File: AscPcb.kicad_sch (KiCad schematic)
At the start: 30 parts, among them J1 USB_C_Receptacle_USB2.0_16P, J2 B2B-PH-K-S, SW1 SW_MEC_5E, SW2 SW_MEC_5E, U1 TLV75801PDRV, U2 BQ24040DSQR, U3 ESP32-C3-WROOM-02

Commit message: schematic first attempt
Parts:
- removed C10, C11: 100nF, Capacitor_SMD:C_0603_1608Metric, symbol Device:C
- removed C12, C5: 20uF, Capacitor_SMD:C_0603_1608Metric, symbol Device:C
- added R10, R11, R12, R9: 10k, Resistor_SMD:R_0603_1608Metric, symbol Device:R
- C8, C9: value C -> 1uF
- SW1: value SW_MEC_5E -> RESET
- SW2: value SW_MEC_5E -> BOOT
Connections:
- net 3V3: now also R10.1, R11.1, R12.2, R9.1
- net GND: now also C8.2, C9.2, SW1.1, SW1.2, SW2.1, SW2.2
- net at C9.1: now also SW2.3 (K), SW2.4 (A), U3.8 (IO9), R10.2
- net at U3.16 (IO2): now also R12.1
- net at U3.2 (EN): now also C8.1, SW1.3 (K), SW1.4 (A), R9.2
- net at U3.7 (IO8): now also R11.2
- net USB_N renamed D-
- net USB_P renamed D+
- no-connect marks 0 -> 15
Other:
- moved on the sheet: C8, C9, SW1, SW2, U3

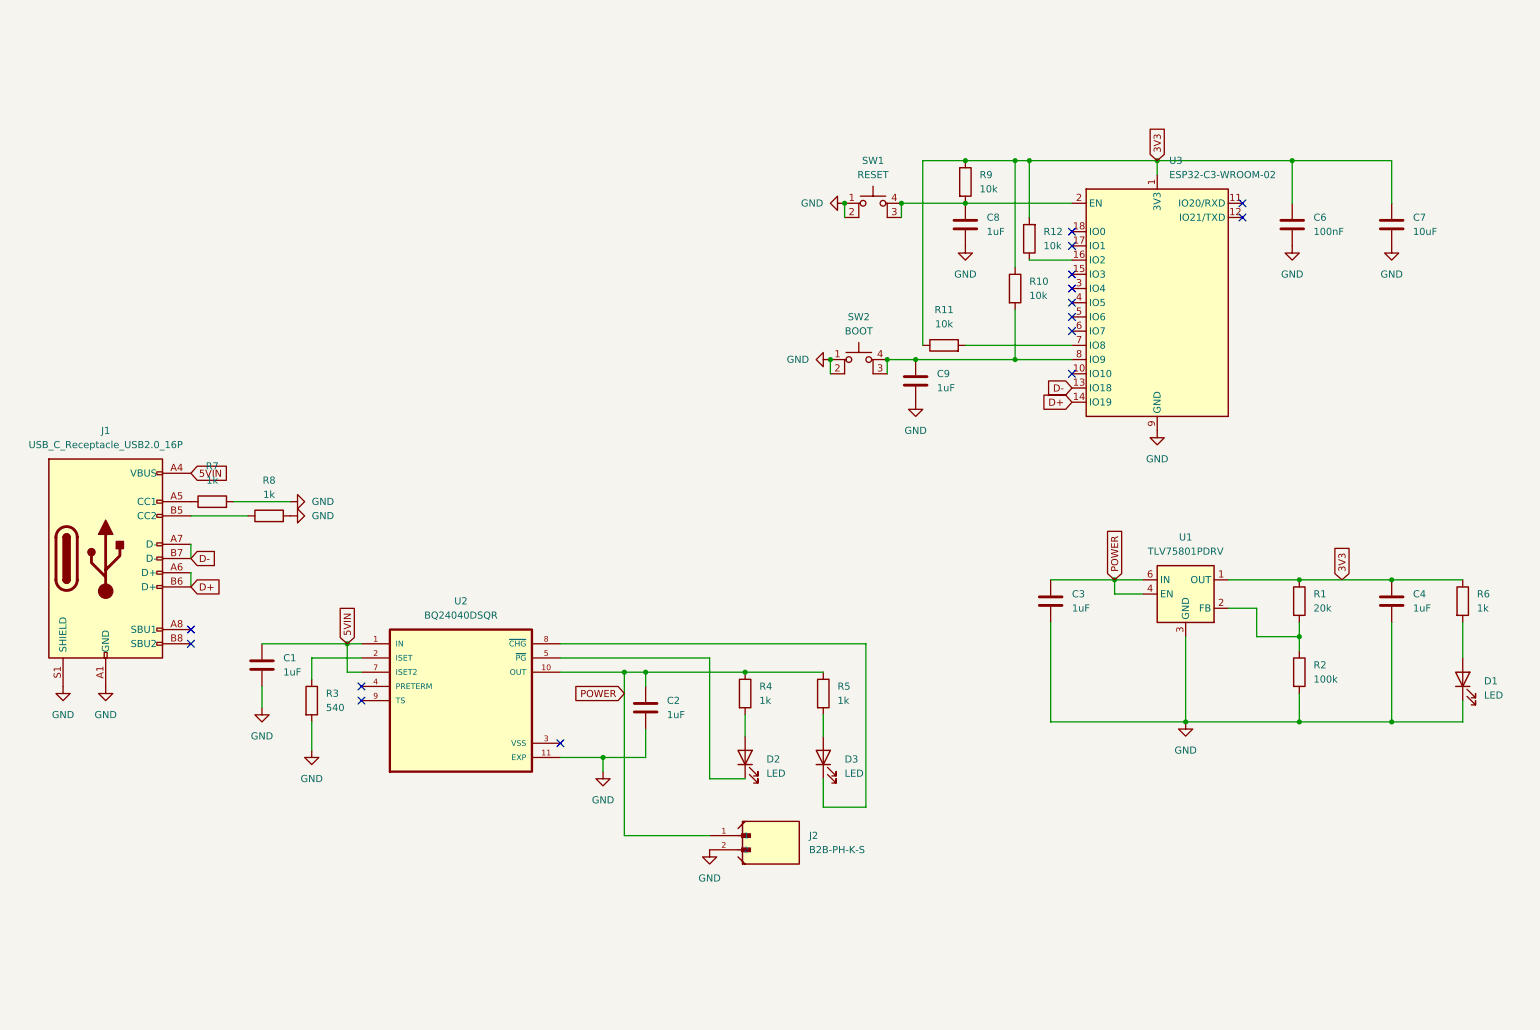
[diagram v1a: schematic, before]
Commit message: inserted actual capacitors
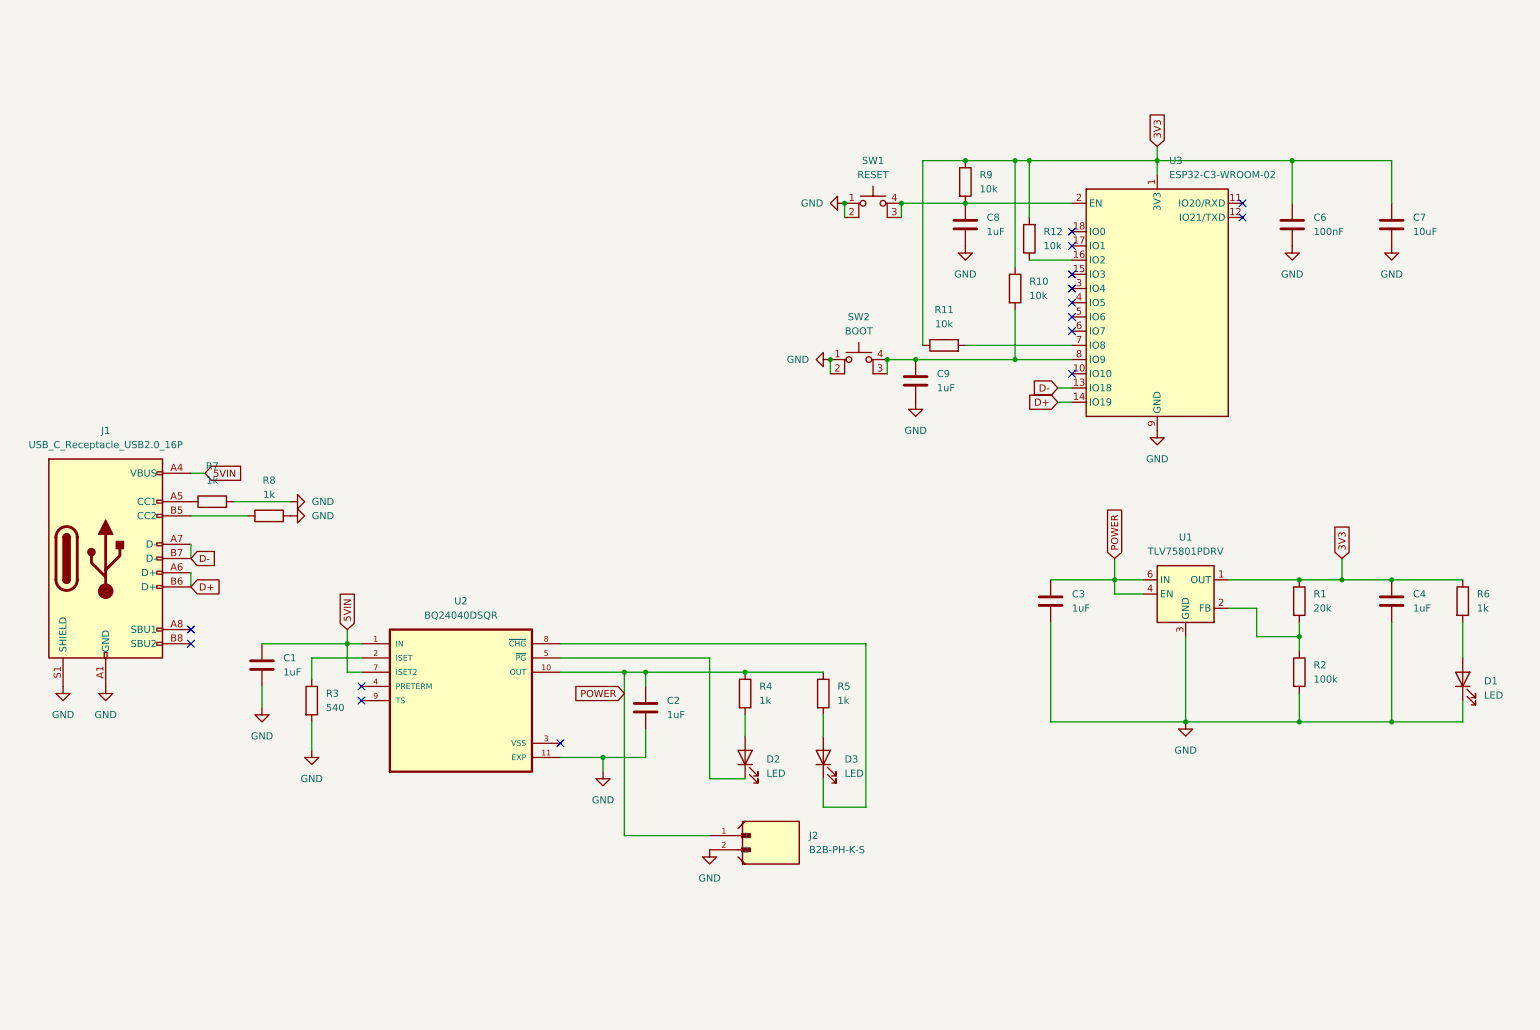
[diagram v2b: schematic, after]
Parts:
- C1, C2, C3, C4, C8, C9: MPN (none) -> CL10B105KP8NNNC
- C6: MPN (none) -> C0603C104K8RACTU
- C7: MPN (none) -> T58MM106M6R3C0500
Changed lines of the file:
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@@
 	)
 	(junction
+		(at 254 119.38)
+		(diameter 0)
+		(color 0 0 0 0)
+	)
+	(junction
 		(at 246.38 119.38)
 		(diameter 0)
@@
 	(wire
 		(pts
+			(xy 254 115.57) (xy 254 119.38)
+		)
+		(stroke
+			(width 0)
+			(type default)
+		)
+	)
+	(wire
+		(pts
 			(xy 246.38 144.78) (xy 246.38 139.7)
 		)
@@
 	(wire
 		(pts
-			(xy 246.38 119.38) (xy 262.89 119.38)
+			(xy 203.2 87.63) (xy 205.74 87.63)
+		)
+		(stroke
+			(width 0)
+			(type default)
+		)
+	)
+	(wire
+		(pts
+			(xy 246.38 119.38) (xy 254 119.38)
 		)
 		(stroke
@@
 	(wire
 		(pts
+			(xy 254 119.38) (xy 262.89 119.38)
+		)
+		(stroke
+			(width 0)
+			(type default)
+		)
+	)
+	(wire
+		(pts
+			(xy 220.98 41.91) (xy 220.98 44.45)
+		)
+		(stroke
+			(width 0)
+			(type default)
+		)
+	)
+	(wire
+		(pts
 			(xy 76.2 130.81) (xy 78.74 130.81)
 		)
@@
 	(wire
 		(pts
+			(xy 50.8 100.33) (xy 48.26 100.33)
+		)
+		(stroke
+			(width 0)
+			(type default)
+		)
+	)
+	(wire
+		(pts
 			(xy 233.68 119.38) (xy 246.38 119.38)
 		)
@@
 	(wire
 		(pts
+			(xy 203.2 85.09) (xy 205.74 85.09)
+		)
+		(stroke
+			(width 0)
+			(type default)
+		)
+	)
+	(wire
+		(pts
 			(xy 129.54 135.89) (xy 147.32 135.89)
 		)
@@
 	(wire
 		(pts
+			(xy 213.36 115.57) (xy 213.36 119.38)
+		)
+		(stroke
+			(width 0)
+			(type default)
+		)
+	)
+	(wire
+		(pts
 			(xy 168.91 160.02) (xy 161.29 160.02)
 		)
@@
 	(wire
 		(pts
+			(xy 76.2 128.27) (xy 76.2 130.81)
+		)
+		(stroke
+			(width 0)
+			(type default)
+		)
+	)
+	(wire
+		(pts
 			(xy 168.91 130.81) (xy 168.91 160.02)
 		)
@@
 	(global_label "D-"
 		(shape input)
-		(at 205.74 85.09 180)
+		(at 203.2 85.09 180)
 		(fields_autoplaced yes)
 		(effects
@@
 		)
 		(property "Intersheetrefs" "${INTERSHEET_REFS}"
-			(at 199.9124 85.09 0)
+			(at 197.3724 85.09 0)
 			(effects
 				(font
@@
 	(global_label "5VIN"
 		(shape input)
-		(at 76.2 130.81 90)
+		(at 76.2 128.27 90)
 		(fields_autoplaced yes)
 		(effects
@@
 		)
 		(property "Intersheetrefs" "${INTERSHEET_REFS}"
-			(at 76.2 123.5914 90)
+			(at 76.2 121.0514 90)
 			(effects
 				(font
@@
 	(global_label "3V3"
 		(shape input)
-		(at 254 119.38 90)
+		(at 254 115.57 90)
 		(fields_autoplaced yes)
 		(effects
@@
 		)
 		(property "Intersheetrefs" "${INTERSHEET_REFS}"
-			(at 254 112.8872 90)
+			(at 254 109.0772 90)
 			(effects
 				(font
@@
 	(global_label "POWER"
 		(shape input)
-		(at 213.36 119.38 90)
+		(at 213.36 115.57 90)
 		(fields_autoplaced yes)
 		(effects
@@
 		)
 		(property "Intersheetrefs" "${INTERSHEET_REFS}"
-			(at 213.36 109.9239 90)
+			(at 213.36 106.1139 90)
 			(effects
 				(font
@@
 	(global_label "3V3"
 		(shape input)
-		(at 220.98 44.45 90)
+		(at 220.98 41.91 90)
 		(fields_autoplaced yes)
 		(effects
@@
 		)
 		(property "Intersheetrefs" "${INTERSHEET_REFS}"
-			(at 220.98 37.9572 90)
+			(at 220.98 35.4172 90)
 			(effects
 				(font
@@
 	(global_label "D+"
 		(shape input)
-		(at 205.74 87.63 180)
+		(at 203.2 87.63 180)
 		(fields_autoplaced yes)
 		(effects
@@
 		)
 		(property "Intersheetrefs" "${INTERSHEET_REFS}"
-			(at 199.9124 87.63 0)
+			(at 197.3724 87.63 0)
 			(effects
 				(font
@@
 	(global_label "5VIN"
 		(shape input)
-		(at 48.26 100.33 0)
+		(at 50.8 100.33 0)
 		(fields_autoplaced yes)
 		(effects
@@
 		)
 		(property "Intersheetrefs" "${INTERSHEET_REFS}"
-			(at 55.4786 100.33 0)
+			(at 58.0186 100.33 0)
 			(effects
 				(font
@@
 			)
 		)
-		(property "Datasheet" "~"
+		(property "Datasheet" "https://www.vishay.com/docs/40189/t58.pdf"
 			(at 262.89 55.88 0)
 			(effects
@@
 			)
 		)
+		(property "MPN" "T58MM106M6R3C0500"
+			(at 262.89 55.88 0)
+			(effects
+				(font
+					(size 1.27 1.27)
+				)
+				(hide yes)
+			)
+		)
 		(pin "1"
 		)
@@
 			)
 		)
-		(property "Datasheet" "~"
+		(property "Datasheet" "https://mm.digikey.com/Volume0/opasdata/d220001/medias/docus/3584/CL10B105KP8NNNC_Spec.pdf"
 			(at 177.8 83.82 0)
 			(effects
@@
 			)
 		)
+		(property "MPN" "CL10B105KP8NNNC"
+			(at 177.8 83.82 0)
+			(effects
+				(font
+					(size 1.27 1.27)
+				)
+				(hide yes)
+			)
+		)
 		(pin "1"
 		)
@@
 			)
 		)
-		(property "Datasheet" "~"
+		(property "Datasheet" "https://mm.digikey.com/Volume0/opasdata/d220001/medias/docus/3584/CL10B105KP8NNNC_Spec.pdf"
 			(at 262.89 123.19 0)
 			(effects
@@
 			)
 		)
+		(property "MPN" "CL10B105KP8NNNC"
+			(at 262.89 123.19 0)
+			(effects
+				(font
+					(size 1.27 1.27)
+				)
+				(hide yes)
+			)
+		)
 		(pin "1"
 		)
@@
 			)
 		)
-		(property "Datasheet" "~"
+		(property "Datasheet" "https://mm.digikey.com/Volume0/opasdata/d220001/medias/docus/3584/CL10B105KP8NNNC_Spec.pdf"
 			(at 60.96 134.62 0)
 			(effects
@@
 			)
 		)
+		(property "MPN" "CL10B105KP8NNNC"
+			(at 60.96 134.62 0)
+			(effects
+				(font
+					(size 1.27 1.27)
+				)
+				(hide yes)
+			)
+		)
 		(pin "1"
 		)
@@
 			)
 		)
-		(property "Datasheet" "~"
+		(property "Datasheet" "https://mm.digikey.com/Volume0/opasdata/d220001/medias/docus/3584/CL10B105KP8NNNC_Spec.pdf"
 			(at 201.93 123.19 0)
 			(effects
@@
 			)
 		)
+		(property "MPN" "CL10B105KP8NNNC"
+			(at 201.93 123.19 0)
+			(effects
+				(font
+					(size 1.27 1.27)
+				)
+				(hide yes)
+			)
+		)
 		(pin "1"
 		)
@@
 			)
 		)
-		(property "Datasheet" "~"
+		(property "Datasheet" "https://www.yageogroup.com/content/datasheet/asset/file/KEM_C1002_X7R_SMD"
 			(at 245.11 55.88 0)
 			(effects
@@
 			)
 		)
+		(property "MPN" "C0603C104K8RACTU"
+			(at 245.11 55.88 0)
+			(effects
+				(font
+					(size 1.27 1.27)
+				)
+				(hide yes)
+			)
+		)
 		(pin "1"
 		)
@@
 			)
 		)
-		(property "Datasheet" "~"
+		(property "Datasheet" "https://mm.digikey.com/Volume0/opasdata/d220001/medias/docus/3584/CL10B105KP8NNNC_Spec.pdf"
 			(at 186.69 55.88 0)
 			(effects
@@
 			)
 		)
+		(property "MPN" "CL10B105KP8NNNC"
+			(at 186.69 55.88 0)
+			(effects
+				(font
+					(size 1.27 1.27)
+				)
+				(hide yes)
+			)
+		)
 		(pin "1"
 		)
@@
 			)
 		)
-		(property "Datasheet" "~"
+		(property "Datasheet" "https://mm.digikey.com/Volume0/opasdata/d220001/medias/docus/3584/CL10B105KP8NNNC_Spec.pdf"
 			(at 129.54 142.24 0)
 			(effects
@@
 			(at 129.54 142.24 0)
 			(effects
+				(font
+					(size 1.27 1.27)
+				)
+				(hide yes)
+			)
+		)
+		(property "MPN" "CL10B105KP8NNNC"
+			(at 129.54 142.24 0)
+			(effects

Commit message: MPN and Datasheets for Resistors and generating BOM
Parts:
- R1: value 20k -> 10k; MPN (none) -> RC0603FR-0710KL
- R10, R11, R12, R9: MPN (none) -> RC0603FR-0710KL
- R2: value 100k -> 49.9k; MPN (none) -> TNPW060349K9BEEA
- R3: value 540 -> 536; MPN (none) -> ERJ-3EKF5360V
- R4, R5, R6, R7, R8: MPN (none) -> CRCW06031K00FKEA
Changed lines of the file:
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@@
 			)
 		)
-		(property "Datasheet" "~"
+		(property "Datasheet" "https://www.yageogroup.com/content/datasheet/asset/file/PYU-RC_GROUP_51_ROHS_L"
 			(at 198.12 58.42 0)
 			(effects
@@
 			)
 		)
+		(property "MPN" "RC0603FR-0710KL"
+			(at 198.12 58.42 0)
+			(effects
+				(font
+					(size 1.27 1.27)
+				)
+				(hide yes)
+			)
+		)
 		(pin "2"
 		)
@@
 			)
 		)
-		(property "Value" "20k"
+		(property "Value" "10k"
 			(at 248.92 124.4599 0)
 			(effects
@@
 			)
 		)
-		(property "Datasheet" "~"
+		(property "Datasheet" "https://www.yageogroup.com/content/datasheet/asset/file/PYU-RC_GROUP_51_ROHS_L"
 			(at 246.38 123.19 0)
 			(effects
@@
 			)
 		)
+		(property "MPN" "RC0603FR-0710KL"
+			(at 246.38 123.19 0)
+			(effects
+				(font
+					(size 1.27 1.27)
+				)
+				(hide yes)
+			)
+		)
 		(pin "2"
 		)
@@
 			)
 		)
-		(property "Datasheet" "~"
+		(property "Datasheet" "https://www.vishay.com/docs/20035/dcrcwe3.pdf"
 			(at 275.59 123.19 0)
 			(effects
@@
 			)
 		)
+		(property "MPN" "CRCW06031K00FKEA"
+			(at 275.59 123.19 0)
+			(effects
+				(font
+					(size 1.27 1.27)
+				)
+				(hide yes)
+			)
+		)
 		(pin "2"
 		)
@@
 			)
 		)
-		(property "Datasheet" "~"
+		(property "Datasheet" "https://www.vishay.com/docs/20035/dcrcwe3.pdf"
 			(at 52.07 105.41 0)
 			(effects
@@
 			)
 		)
+		(property "MPN" "CRCW06031K00FKEA"
+			(at 52.07 105.41 90)
+			(effects
+				(font
+					(size 1.27 1.27)
+				)
+				(hide yes)
+			)
+		)
 		(pin "2"
 		)
@@
 			)
 		)
-		(property "Datasheet" "~"
+		(property "Datasheet" "https://www.yageogroup.com/content/datasheet/asset/file/PYU-RC_GROUP_51_ROHS_L"
 			(at 195.58 67.31 0)
 			(effects
@@
 			)
 		)
+		(property "MPN" "RC0603FR-0710KL"
+			(at 195.58 67.31 0)
+			(effects
+				(font
+					(size 1.27 1.27)
+				)
+				(hide yes)
+			)
+		)
 		(pin "2"
 		)
@@
 			)
 		)
-		(property "Datasheet" "~"
+		(property "Datasheet" "https://www.vishay.com/docs/20035/dcrcwe3.pdf"
 			(at 161.29 139.7 0)
 			(effects
@@
 			)
 		)
+		(property "MPN" "CRCW06031K00FKEA"
+			(at 161.29 139.7 0)
+			(effects
+				(font
+					(size 1.27 1.27)
+				)
+				(hide yes)
+			)
+		)
 		(pin "2"
 		)
@@
 			)
 		)
-		(property "Datasheet" "~"
+		(property "Datasheet" "https://www.yageogroup.com/content/datasheet/asset/file/PYU-RC_GROUP_51_ROHS_L"
 			(at 182.88 77.47 0)
 			(effects
@@
 			)
 		)
+		(property "MPN" "RC0603FR-0710KL"
+			(at 182.88 77.47 90)
+			(effects
+				(font
+					(size 1.27 1.27)
+				)
+				(hide yes)
+			)
+		)
 		(pin "2"
 		)
@@
 			)
 		)
-		(property "Value" "540"
+		(property "Value" "536"
 			(at 72.39 142.2399 0)
 			(effects
@@
 			)
 		)
-		(property "Datasheet" "~"
+		(property "Datasheet" "https://industrial.panasonic.com/cdbs/www-data/pdf/RDA0000/AOA0000C304.pdf"
 			(at 69.85 140.97 0)
 			(effects
@@
 			)
 		)
+		(property "MPN" "ERJ-3EKF5360V"
+			(at 69.85 140.97 0)
+			(effects
+				(font
+					(size 1.27 1.27)
+				)
+				(hide yes)
+			)
+		)
 		(pin "2"
 		)
@@
 			)
 		)
-		(property "Datasheet" "~"
+		(property "Datasheet" "https://www.vishay.com/docs/20035/dcrcwe3.pdf"
 			(at 147.32 139.7 0)
 			(effects
@@
 			)
 		)
+		(property "MPN" "CRCW06031K00FKEA"
+			(at 147.32 139.7 0)
+			(effects
+				(font
+					(size 1.27 1.27)
+				)
+				(hide yes)
+			)
+		)
 		(pin "2"
 		)
@@
 			)
 		)
-		(property "Value" "100k"
+		(property "Value" "49.9k"
 			(at 248.92 137.1599 0)
 			(effects
@@
 			)
 		)
-		(property "Datasheet" "~"
+		(property "Datasheet" "https://www.vishay.com/docs/28758/tnpw_e3.pdf"
 			(at 246.38 135.89 0)
 			(effects
@@
 			)
 		)
+		(property "MPN" "TNPW060349K9BEEA"
+			(at 246.38 135.89 0)
+			(effects
+				(font
+					(size 1.27 1.27)
+				)
+				(hide yes)
+			)
+		)
 		(pin "2"
 		)
@@
 			)
 		)
-		(property "Datasheet" "~"
+		(property "Datasheet" "https://www.vishay.com/docs/20035/dcrcwe3.pdf"
 			(at 62.23 107.95 0)
 			(effects
@@
 			)
 		)
+		(property "MPN" "CRCW06031K00FKEA"
+			(at 62.23 107.95 90)
+			(effects
+				(font
+					(size 1.27 1.27)
+				)
+				(hide yes)
+			)
+		)
 		(pin "2"
 		)
@@
 			)
 		)
-		(property "Datasheet" "~"
+		(property "Datasheet" "https://www.yageogroup.com/content/datasheet/asset/file/PYU-RC_GROUP_51_ROHS_L"
 			(at 186.69 48.26 0)
 			(effects
@@
 			(at 186.69 48.26 0)
 			(effects
+				(font
+					(size 1.27 1.27)
+				)
+				(hide yes)
+			)
+		)
+		(property "MPN" "RC0603FR-0710KL"
+			(at 186.69 48.26 0)
+			(effects
